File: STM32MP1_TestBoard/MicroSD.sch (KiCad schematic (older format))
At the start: 6 parts

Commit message: updated bom, readme
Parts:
- J11: renamed from J?; Mfr (none) -> Molex; PartNo (none) -> 475710001
- gave numbers to parts that had none: 5
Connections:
- net labels removed: GNDPWR
- wire segments 35 -> 34
- no-connect marks 0 -> 1
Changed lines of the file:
@@
 $Descr A4 11693 8268
 encoding utf-8
-Sheet 7 9
+Sheet 8 9
 Title ""
 Date ""
@@
 	7100 1975 7100 3725
 $Comp
-L power:+3.3V #PWR?
+L power:+3.3V #PWR0120
 U 1 1 5FB10145
 P 7100 1975
-AR Path="/60F0FA94/5FB10145" Ref="#PWR?"  Part="1"
+AR Path="/60F0FA94/5FB10145" Ref="#PWR0120"  Part="1"
 AR Path="/60F1156A/5FB10145" Ref="#PWR?"  Part="1"
-AR Path="/60F2D08D/5FB10145" Ref="#PWR?"  Part="1"
-F 0 "#PWR?" H 7100 1825 50  0001 C CNN
+AR Path="/60F2D08D/5FB10145" Ref="#PWR0124"  Part="1"
+F 0 "#PWR0124" H 7100 1825 50  0001 C CNN
 F 1 "+3.3V" H 7115 2148 50  0000 C CNN
 F 2 "" H 7100 1975 50  0001 C CNN
@@
 	6900 1975 6900 3725
 $Comp
-L power:GNDS #PWR?
+L power:GNDS #PWR0121
 U 1 1 5FB10A8F
 P 6900 1975
-AR Path="/60F0FA94/5FB10A8F" Ref="#PWR?"  Part="1"
+AR Path="/60F0FA94/5FB10A8F" Ref="#PWR0121"  Part="1"
 AR Path="/60F1156A/5FB10A8F" Ref="#PWR?"  Part="1"
-AR Path="/60F2D08D/5FB10A8F" Ref="#PWR?"  Part="1"
-F 0 "#PWR?" H 6900 1725 50  0001 C CNN
+AR Path="/60F2D08D/5FB10A8F" Ref="#PWR0125"  Part="1"
+F 0 "#PWR0125" H 6900 1725 50  0001 C CNN
 F 1 "GNDS" H 6905 1802 50  0000 C CNN
 F 2 "" H 6900 1975 50  0001 C CNN
@@
 $EndComp
 $Comp
-L Device:R R?
+L Device:R R40
 U 1 1 5FB12D8F
 P 4550 1725
-AR Path="/60F0FA94/5FB12D8F" Ref="R?"  Part="1"
+AR Path="/60F0FA94/5FB12D8F" Ref="R40"  Part="1"
 AR Path="/60F1156A/5FB12D8F" Ref="R?"  Part="1"
-AR Path="/60F2D08D/5FB12D8F" Ref="R?"  Part="1"
-F 0 "R?" H 4620 1771 50  0000 L CNN
+AR Path="/60F2D08D/5FB12D8F" Ref="R45"  Part="1"
+F 0 "R45" H 4620 1771 50  0000 L CNN
 F 1 "47K" H 4620 1680 50  0000 L CNN
 F 2 "Resistor_SMD:R_0805_2012Metric_Pad1.15x1.40mm_HandSolder" V 4480 1725 50  0001 C CNN
 F 3 "~" H 4550 1725 50  0001 C CNN
+F 4 "~" H 4550 1725 50  0001 C CNN "Mfr"
+F 5 "~" H 4550 1725 50  0001 C CNN "PartNo"
 	1    4550 1725
 	1    0    0    -1
 $EndComp
 $Comp
-L Device:R R?
+L Device:R R41
 U 1 1 5FB155D6
 P 4925 1725
-AR Path="/60F0FA94/5FB155D6" Ref="R?"  Part="1"
+AR Path="/60F0FA94/5FB155D6" Ref="R41"  Part="1"
 AR Path="/60F1156A/5FB155D6" Ref="R?"  Part="1"
-AR Path="/60F2D08D/5FB155D6" Ref="R?"  Part="1"
-F 0 "R?" H 4995 1771 50  0000 L CNN
+AR Path="/60F2D08D/5FB155D6" Ref="R46"  Part="1"
+F 0 "R46" H 4995 1771 50  0000 L CNN
 F 1 "47K" H 4995 1680 50  0000 L CNN
 F 2 "Resistor_SMD:R_0805_2012Metric_Pad1.15x1.40mm_HandSolder" V 4855 1725 50  0001 C CNN
 F 3 "~" H 4925 1725 50  0001 C CNN
+F 4 "~" H 4925 1725 50  0001 C CNN "Mfr"
+F 5 "~" H 4925 1725 50  0001 C CNN "PartNo"
 	1    4925 1725
 	1    0    0    -1
 $EndComp
 $Comp
-L Device:R R?
+L Device:R R42
 U 1 1 5FB158C2
 P 5275 1725
-AR Path="/60F0FA94/5FB158C2" Ref="R?"  Part="1"
+AR Path="/60F0FA94/5FB158C2" Ref="R42"  Part="1"
 AR Path="/60F1156A/5FB158C2" Ref="R?"  Part="1"
-AR Path="/60F2D08D/5FB158C2" Ref="R?"  Part="1"
-F 0 "R?" H 5345 1771 50  0000 L CNN
+AR Path="/60F2D08D/5FB158C2" Ref="R47"  Part="1"
+F 0 "R47" H 5345 1771 50  0000 L CNN
 F 1 "47K" H 5345 1680 50  0000 L CNN
 F 2 "Resistor_SMD:R_0805_2012Metric_Pad1.15x1.40mm_HandSolder" V 5205 1725 50  0001 C CNN
 F 3 "~" H 5275 1725 50  0001 C CNN
+F 4 "~" H 5275 1725 50  0001 C CNN "Mfr"
+F 5 "~" H 5275 1725 50  0001 C CNN "PartNo"
 	1    5275 1725
 	1    0    0    -1
 $EndComp
 $Comp
-L Device:R R?
+L Device:R R43
 U 1 1 5FB15A9B
 P 5625 1725
-AR Path="/60F0FA94/5FB15A9B" Ref="R?"  Part="1"
+AR Path="/60F0FA94/5FB15A9B" Ref="R43"  Part="1"
 AR Path="/60F1156A/5FB15A9B" Ref="R?"  Part="1"
-AR Path="/60F2D08D/5FB15A9B" Ref="R?"  Part="1"
-F 0 "R?" H 5695 1771 50  0000 L CNN
+AR Path="/60F2D08D/5FB15A9B" Ref="R48"  Part="1"
+F 0 "R48" H 5695 1771 50  0000 L CNN
 F 1 "47K" H 5695 1680 50  0000 L CNN
 F 2 "Resistor_SMD:R_0805_2012Metric_Pad1.15x1.40mm_HandSolder" V 5555 1725 50  0001 C CNN
 F 3 "~" H 5625 1725 50  0001 C CNN
+F 4 "~" H 5625 1725 50  0001 C CNN "Mfr"
+F 5 "~" H 5625 1725 50  0001 C CNN "PartNo"
 	1    5625 1725
 	1    0    0    -1
 $EndComp
 $Comp
-L Device:R R?
+L Device:R R44
 U 1 1 5FB15D60
 P 5975 1725
-AR Path="/60F0FA94/5FB15D60" Ref="R?"  Part="1"
+AR Path="/60F0FA94/5FB15D60" Ref="R44"  Part="1"
 AR Path="/60F1156A/5FB15D60" Ref="R?"  Part="1"
-AR Path="/60F2D08D/5FB15D60" Ref="R?"  Part="1"
-F 0 "R?" H 6045 1771 50  0000 L CNN
+AR Path="/60F2D08D/5FB15D60" Ref="R49"  Part="1"
+F 0 "R49" H 6045 1771 50  0000 L CNN
 F 1 "47K" H 6045 1680 50  0000 L CNN
 F 2 "Resistor_SMD:R_0805_2012Metric_Pad1.15x1.40mm_HandSolder" V 5905 1725 50  0001 C CNN
 F 3 "~" H 5975 1725 50  0001 C CNN
+F 4 "~" H 5975 1725 50  0001 C CNN "Mfr"
+F 5 "~" H 5975 1725 50  0001 C CNN "PartNo"
 	1    5975 1725
 	1    0    0    -1
@@
 	5275 1375 5275 1225
 $Comp
-L power:+3.3V #PWR?
+L power:+3.3V #PWR0122
 U 1 1 5FB1A870
 P 5275 1225
-AR Path="/60F0FA94/5FB1A870" Ref="#PWR?"  Part="1"
+AR Path="/60F0FA94/5FB1A870" Ref="#PWR0122"  Part="1"
 AR Path="/60F1156A/5FB1A870" Ref="#PWR?"  Part="1"
-AR Path="/60F2D08D/5FB1A870" Ref="#PWR?"  Part="1"
-F 0 "#PWR?" H 5275 1075 50  0001 C CNN
+AR Path="/60F2D08D/5FB1A870" Ref="#PWR0126"  Part="1"
+F 0 "#PWR0126" H 5275 1075 50  0001 C CNN
 F 1 "+3.3V" H 5290 1398 50  0000 C CNN
 F 2 "" H 5275 1225 50  0001 C CNN
@@
 	1    0    0    -1
 $EndComp
-Wire Wire Line
-	6500 5425 6500 5675
-$Comp
-L power:GNDPWR #PWR?
-U 1 1 5FB246F5
-P 6500 5675
-AR Path="/60F0FA94/5FB246F5" Ref="#PWR?"  Part="1"
-AR Path="/60F1156A/5FB246F5" Ref="#PWR?"  Part="1"
-AR Path="/60F2D08D/5FB246F5" Ref="#PWR?"  Part="1"
-F 0 "#PWR?" H 6500 5475 50  0001 C CNN
-F 1 "GNDPWR" H 6504 5521 50  0000 C CNN
-F 2 "" H 6500 5625 50  0001 C CNN
-F 3 "" H 6500 5625 50  0001 C CNN
-	1    6500 5675
-	1    0    0    -1
-$EndComp
-$Comp
-L Connector:Micro_SD_Card J?
+$Comp
+L Connector:Micro_SD_Card J11
 U 1 1 5FA9DE35
 P 7100 4625
-AR Path="/60F0FA94/5FA9DE35" Ref="J?"  Part="1"
+AR Path="/60F0FA94/5FA9DE35" Ref="J11"  Part="1"
 AR Path="/60F1156A/5FA9DE35" Ref="J?"  Part="1"
-AR Path="/60F2D08D/5FA9DE35" Ref="J?"  Part="1"
-F 0 "J?" V 7004 5205 50  0000 L CNN
+AR Path="/60F2D08D/5FA9DE35" Ref="J12"  Part="1"
+F 0 "J12" V 7004 5205 50  0000 L CNN
 F 1 "Micro_SD_Card" V 7095 5205 50  0000 L CNN
 F 2 "Molex_SDIO:Molex_SDIO_475710001" H 8250 4925 50  0001 C CNN
 F 3 "https://www.molex.com/molex/products/part-detail/memory_card_socket/0475710001" H 7100 4625 50  0001 C CNN
+F 4 "Molex" H 7100 4625 50  0001 C CNN "Mfr"
+F 5 "475710001" H 7100 4625 50  0001 C CNN "PartNo"
 	1    7100 4625
 	0    1    1    0
 $EndComp
+NoConn ~ 6500 5425
 $EndSCHEMATC

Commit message: updated netlist
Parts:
- R40, R41, R42, R43, R44: footprint Resistor_SMD:R_0805_2012Metric_Pad1.15x1.40mm_HandSolder -> Resistor_SMD:R_0805_2012Metric_Pad1.20x1.40mm_HandSolder
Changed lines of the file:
@@
 F 0 "R45" H 4620 1771 50  0000 L CNN
 F 1 "47K" H 4620 1680 50  0000 L CNN
-F 2 "Resistor_SMD:R_0805_2012Metric_Pad1.15x1.40mm_HandSolder" V 4480 1725 50  0001 C CNN
+F 2 "Resistor_SMD:R_0805_2012Metric_Pad1.20x1.40mm_HandSolder" V 4480 1725 50  0001 C CNN
 F 3 "~" H 4550 1725 50  0001 C CNN
 F 4 "~" H 4550 1725 50  0001 C CNN "Mfr"
@@
 F 0 "R46" H 4995 1771 50  0000 L CNN
 F 1 "47K" H 4995 1680 50  0000 L CNN
-F 2 "Resistor_SMD:R_0805_2012Metric_Pad1.15x1.40mm_HandSolder" V 4855 1725 50  0001 C CNN
+F 2 "Resistor_SMD:R_0805_2012Metric_Pad1.20x1.40mm_HandSolder" V 4855 1725 50  0001 C CNN
 F 3 "~" H 4925 1725 50  0001 C CNN
 F 4 "~" H 4925 1725 50  0001 C CNN "Mfr"
@@
 F 0 "R47" H 5345 1771 50  0000 L CNN
 F 1 "47K" H 5345 1680 50  0000 L CNN
-F 2 "Resistor_SMD:R_0805_2012Metric_Pad1.15x1.40mm_HandSolder" V 5205 1725 50  0001 C CNN
+F 2 "Resistor_SMD:R_0805_2012Metric_Pad1.20x1.40mm_HandSolder" V 5205 1725 50  0001 C CNN
 F 3 "~" H 5275 1725 50  0001 C CNN
 F 4 "~" H 5275 1725 50  0001 C CNN "Mfr"
@@
 F 0 "R48" H 5695 1771 50  0000 L CNN
 F 1 "47K" H 5695 1680 50  0000 L CNN
-F 2 "Resistor_SMD:R_0805_2012Metric_Pad1.15x1.40mm_HandSolder" V 5555 1725 50  0001 C CNN
+F 2 "Resistor_SMD:R_0805_2012Metric_Pad1.20x1.40mm_HandSolder" V 5555 1725 50  0001 C CNN
 F 3 "~" H 5625 1725 50  0001 C CNN
 F 4 "~" H 5625 1725 50  0001 C CNN "Mfr"
@@
 F 0 "R49" H 6045 1771 50  0000 L CNN
 F 1 "47K" H 6045 1680 50  0000 L CNN
-F 2 "Resistor_SMD:R_0805_2012Metric_Pad1.15x1.40mm_HandSolder" V 5905 1725 50  0001 C CNN
+F 2 "Resistor_SMD:R_0805_2012Metric_Pad1.20x1.40mm_HandSolder" V 5905 1725 50  0001 C CNN
 F 3 "~" H 5975 1725 50  0001 C CNN
 F 4 "~" H 5975 1725 50  0001 C CNN "Mfr"

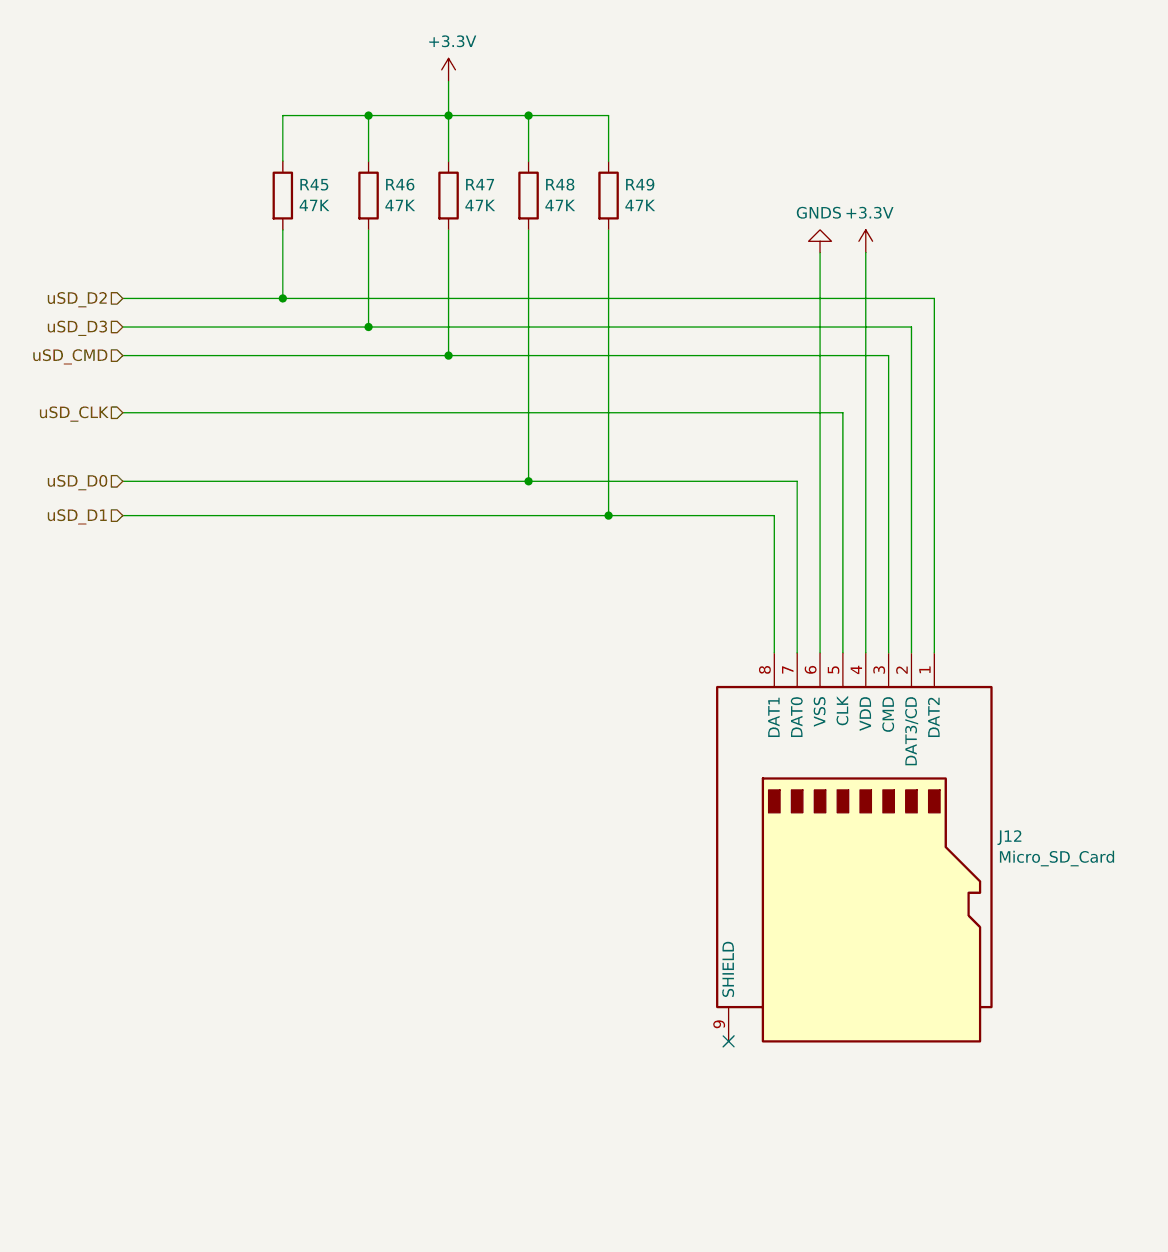
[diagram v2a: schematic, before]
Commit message: updated schematic design
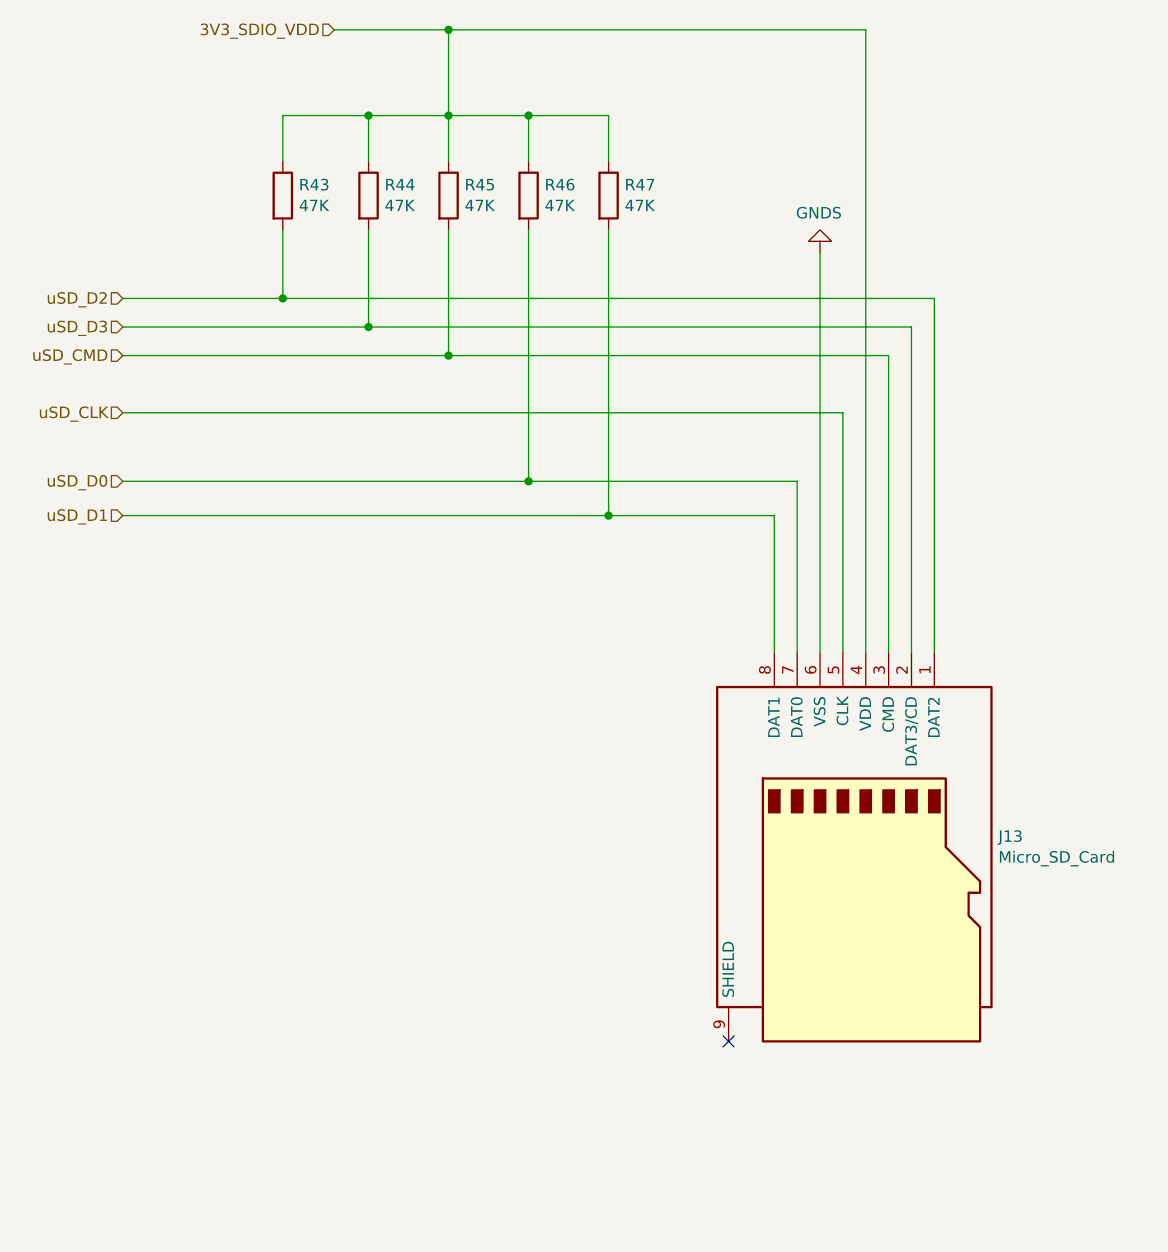
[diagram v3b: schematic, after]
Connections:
- net +3V3 renamed 3V3_SDIO_VDD
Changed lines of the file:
@@
 $Descr A4 11693 8268
 encoding utf-8
-Sheet 8 9
+Sheet 10 10
 Title ""
 Date ""
@@
 	6700 3725 6700 3125
 Wire Wire Line
-	7100 1975 7100 3725
-$Comp
-L power:+3.3V #PWR0120
-U 1 1 5FB10145
-P 7100 1975
-AR Path="/60F0FA94/5FB10145" Ref="#PWR0120"  Part="1"
-AR Path="/60F1156A/5FB10145" Ref="#PWR?"  Part="1"
-AR Path="/60F2D08D/5FB10145" Ref="#PWR0124"  Part="1"
-F 0 "#PWR0124" H 7100 1825 50  0001 C CNN
-F 1 "+3.3V" H 7115 2148 50  0000 C CNN
-F 2 "" H 7100 1975 50  0001 C CNN
-F 3 "" H 7100 1975 50  0001 C CNN
-	1    7100 1975
-	1    0    0    -1
-$EndComp
-Wire Wire Line
 	6900 1975 6900 3725
 $Comp
@@
 AR Path="/60F1156A/5FB10A8F" Ref="#PWR?"  Part="1"
 AR Path="/60F2D08D/5FB10A8F" Ref="#PWR0125"  Part="1"
-F 0 "#PWR0125" H 6900 1725 50  0001 C CNN
+AR Path="/6097C138/60998974/5FB10A8F" Ref="#PWR027"  Part="1"
+AR Path="/6097C138/6099897C/5FB10A8F" Ref="#PWR045"  Part="1"
+AR Path="/6097C138/60E05EB1/5FB10A8F" Ref="#PWR0101"  Part="1"
+F 0 "#PWR0101" H 6900 1725 50  0001 C CNN
 F 1 "GNDS" H 6905 1802 50  0000 C CNN
 F 2 "" H 6900 1975 50  0001 C CNN
@@
 AR Path="/60F1156A/5FB12D8F" Ref="R?"  Part="1"
 AR Path="/60F2D08D/5FB12D8F" Ref="R45"  Part="1"
-F 0 "R45" H 4620 1771 50  0000 L CNN
+AR Path="/6097C138/60998974/5FB12D8F" Ref="R12"  Part="1"
+AR Path="/6097C138/6099897C/5FB12D8F" Ref="R43"  Part="1"
+AR Path="/6097C138/60E05EB1/5FB12D8F" Ref="R43"  Part="1"
+F 0 "R43" H 4620 1771 50  0000 L CNN
 F 1 "47K" H 4620 1680 50  0000 L CNN
 F 2 "Resistor_SMD:R_0805_2012Metric_Pad1.20x1.40mm_HandSolder" V 4480 1725 50  0001 C CNN
@@
 AR Path="/60F1156A/5FB155D6" Ref="R?"  Part="1"
 AR Path="/60F2D08D/5FB155D6" Ref="R46"  Part="1"
-F 0 "R46" H 4995 1771 50  0000 L CNN
+AR Path="/6097C138/60998974/5FB155D6" Ref="R13"  Part="1"
+AR Path="/6097C138/6099897C/5FB155D6" Ref="R44"  Part="1"
+AR Path="/6097C138/60E05EB1/5FB155D6" Ref="R44"  Part="1"
+F 0 "R44" H 4995 1771 50  0000 L CNN
 F 1 "47K" H 4995 1680 50  0000 L CNN
 F 2 "Resistor_SMD:R_0805_2012Metric_Pad1.20x1.40mm_HandSolder" V 4855 1725 50  0001 C CNN
@@
 AR Path="/60F1156A/5FB158C2" Ref="R?"  Part="1"
 AR Path="/60F2D08D/5FB158C2" Ref="R47"  Part="1"
-F 0 "R47" H 5345 1771 50  0000 L CNN
+AR Path="/6097C138/60998974/5FB158C2" Ref="R40"  Part="1"
+AR Path="/6097C138/6099897C/5FB158C2" Ref="R45"  Part="1"
+AR Path="/6097C138/60E05EB1/5FB158C2" Ref="R45"  Part="1"
+F 0 "R45" H 5345 1771 50  0000 L CNN
 F 1 "47K" H 5345 1680 50  0000 L CNN
 F 2 "Resistor_SMD:R_0805_2012Metric_Pad1.20x1.40mm_HandSolder" V 5205 1725 50  0001 C CNN
@@
 AR Path="/60F1156A/5FB15A9B" Ref="R?"  Part="1"
 AR Path="/60F2D08D/5FB15A9B" Ref="R48"  Part="1"
-F 0 "R48" H 5695 1771 50  0000 L CNN
+AR Path="/6097C138/60998974/5FB15A9B" Ref="R41"  Part="1"
+AR Path="/6097C138/6099897C/5FB15A9B" Ref="R46"  Part="1"
+AR Path="/6097C138/60E05EB1/5FB15A9B" Ref="R46"  Part="1"
+F 0 "R46" H 5695 1771 50  0000 L CNN
 F 1 "47K" H 5695 1680 50  0000 L CNN
 F 2 "Resistor_SMD:R_0805_2012Metric_Pad1.20x1.40mm_HandSolder" V 5555 1725 50  0001 C CNN
@@
 AR Path="/60F1156A/5FB15D60" Ref="R?"  Part="1"
 AR Path="/60F2D08D/5FB15D60" Ref="R49"  Part="1"
-F 0 "R49" H 6045 1771 50  0000 L CNN
+AR Path="/6097C138/60998974/5FB15D60" Ref="R42"  Part="1"
+AR Path="/6097C138/6099897C/5FB15D60" Ref="R47"  Part="1"
+AR Path="/6097C138/60E05EB1/5FB15D60" Ref="R47"  Part="1"
+F 0 "R47" H 6045 1771 50  0000 L CNN
 F 1 "47K" H 6045 1680 50  0000 L CNN
 F 2 "Resistor_SMD:R_0805_2012Metric_Pad1.20x1.40mm_HandSolder" V 5905 1725 50  0001 C CNN
@@
 Wire Wire Line
 	4925 1375 5275 1375
-Wire Wire Line
-	5275 1375 5275 1225
-$Comp
-L power:+3.3V #PWR0122
-U 1 1 5FB1A870
-P 5275 1225
-AR Path="/60F0FA94/5FB1A870" Ref="#PWR0122"  Part="1"
-AR Path="/60F1156A/5FB1A870" Ref="#PWR?"  Part="1"
-AR Path="/60F2D08D/5FB1A870" Ref="#PWR0126"  Part="1"
-F 0 "#PWR0126" H 5275 1075 50  0001 C CNN
-F 1 "+3.3V" H 5290 1398 50  0000 C CNN
-F 2 "" H 5275 1225 50  0001 C CNN
-F 3 "" H 5275 1225 50  0001 C CNN
-	1    5275 1225
-	1    0    0    -1
-$EndComp
 $Comp
 L Connector:Micro_SD_Card J11
@@
 AR Path="/60F1156A/5FA9DE35" Ref="J?"  Part="1"
 AR Path="/60F2D08D/5FA9DE35" Ref="J12"  Part="1"
-F 0 "J12" V 7004 5205 50  0000 L CNN
+AR Path="/6097C138/60998974/5FA9DE35" Ref="J12"  Part="1"
+AR Path="/6097C138/6099897C/5FA9DE35" Ref="J13"  Part="1"
+AR Path="/6097C138/60E05EB1/5FA9DE35" Ref="J13"  Part="1"
+F 0 "J13" V 7004 5205 50  0000 L CNN
 F 1 "Micro_SD_Card" V 7095 5205 50  0000 L CNN
 F 2 "Molex_SDIO:Molex_SDIO_475710001" H 8250 4925 50  0001 C CNN
@@
 $EndComp
 NoConn ~ 6500 5425
+Text HLabel 4775 1000 0    50   Input ~ 0
+3V3_SDIO_VDD
+Wire Wire Line
+	5275 1000 4775 1000
+Wire Wire Line
+	5275 1000 5275 1375
+Wire Wire Line
+	7100 1000 5275 1000
+Wire Wire Line
+	7100 1000 7100 3725
+Connection ~ 5275 1000
 $EndSCHEMATC

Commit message: layout update
backup. work in progress
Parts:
- R40, R41, R42, R43, R44: footprint Resistor_SMD:R_0805_2012Metric_Pad1.20x1.40mm_HandSolder -> Resistor_SMD:R_0402_1005Metric_Pad0.72x0.64mm_HandSolder
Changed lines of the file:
@@
 $Descr A4 11693 8268
 encoding utf-8
-Sheet 10 10
+Sheet 9 10
 Title ""
 Date ""
@@
 F 0 "R43" H 4620 1771 50  0000 L CNN
 F 1 "47K" H 4620 1680 50  0000 L CNN
-F 2 "Resistor_SMD:R_0805_2012Metric_Pad1.20x1.40mm_HandSolder" V 4480 1725 50  0001 C CNN
+F 2 "Resistor_SMD:R_0402_1005Metric_Pad0.72x0.64mm_HandSolder" V 4480 1725 50  0001 C CNN
 F 3 "~" H 4550 1725 50  0001 C CNN
 F 4 "~" H 4550 1725 50  0001 C CNN "Mfr"
@@
 F 0 "R44" H 4995 1771 50  0000 L CNN
 F 1 "47K" H 4995 1680 50  0000 L CNN
-F 2 "Resistor_SMD:R_0805_2012Metric_Pad1.20x1.40mm_HandSolder" V 4855 1725 50  0001 C CNN
+F 2 "Resistor_SMD:R_0402_1005Metric_Pad0.72x0.64mm_HandSolder" V 4855 1725 50  0001 C CNN
 F 3 "~" H 4925 1725 50  0001 C CNN
 F 4 "~" H 4925 1725 50  0001 C CNN "Mfr"
@@
 F 0 "R45" H 5345 1771 50  0000 L CNN
 F 1 "47K" H 5345 1680 50  0000 L CNN
-F 2 "Resistor_SMD:R_0805_2012Metric_Pad1.20x1.40mm_HandSolder" V 5205 1725 50  0001 C CNN
+F 2 "Resistor_SMD:R_0402_1005Metric_Pad0.72x0.64mm_HandSolder" V 5205 1725 50  0001 C CNN
 F 3 "~" H 5275 1725 50  0001 C CNN
 F 4 "~" H 5275 1725 50  0001 C CNN "Mfr"
@@
 F 0 "R46" H 5695 1771 50  0000 L CNN
 F 1 "47K" H 5695 1680 50  0000 L CNN
-F 2 "Resistor_SMD:R_0805_2012Metric_Pad1.20x1.40mm_HandSolder" V 5555 1725 50  0001 C CNN
+F 2 "Resistor_SMD:R_0402_1005Metric_Pad0.72x0.64mm_HandSolder" V 5555 1725 50  0001 C CNN
 F 3 "~" H 5625 1725 50  0001 C CNN
 F 4 "~" H 5625 1725 50  0001 C CNN "Mfr"
@@
 F 0 "R47" H 6045 1771 50  0000 L CNN
 F 1 "47K" H 6045 1680 50  0000 L CNN
-F 2 "Resistor_SMD:R_0805_2012Metric_Pad1.20x1.40mm_HandSolder" V 5905 1725 50  0001 C CNN
+F 2 "Resistor_SMD:R_0402_1005Metric_Pad0.72x0.64mm_HandSolder" V 5905 1725 50  0001 C CNN
 F 3 "~" H 5975 1725 50  0001 C CNN
 F 4 "~" H 5975 1725 50  0001 C CNN "Mfr"
